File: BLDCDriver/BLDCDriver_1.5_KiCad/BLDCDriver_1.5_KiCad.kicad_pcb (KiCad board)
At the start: 2 copper layers, 42 x 43.2 mm, 72 parts, among them IC1 STSPIN32G4, J2 Debug, J3 FFC_11P_1mm, J4 POWER, J5 CAN, SW1 SW_Push, U4 MCP2562-E-SN, U5 AS5048A-HTSP-500, U6 AP7375-50SA

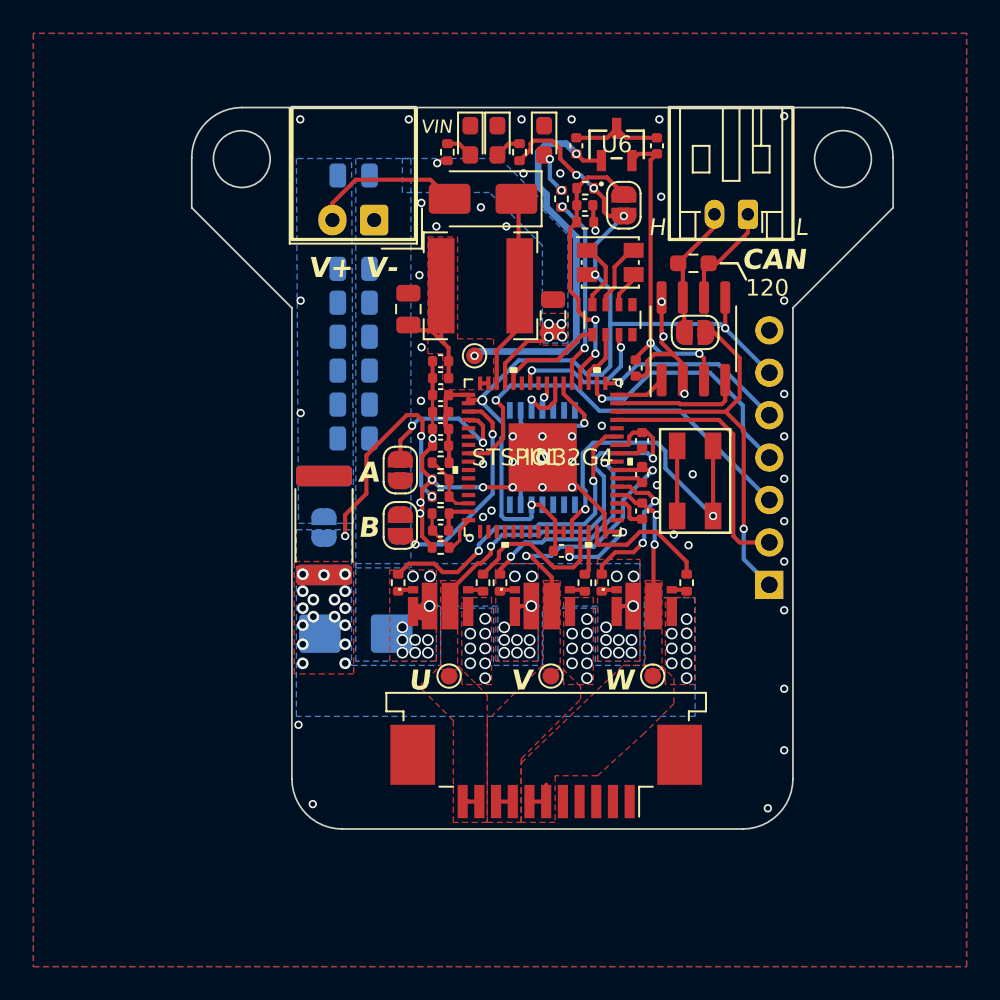
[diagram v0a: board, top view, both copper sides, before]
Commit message: ⚠️電源のシルク逆、SPI_CS繋がってないのを修正、GNDベタ最適化、Production
結構気づかなかったらやばかったやつばっかり
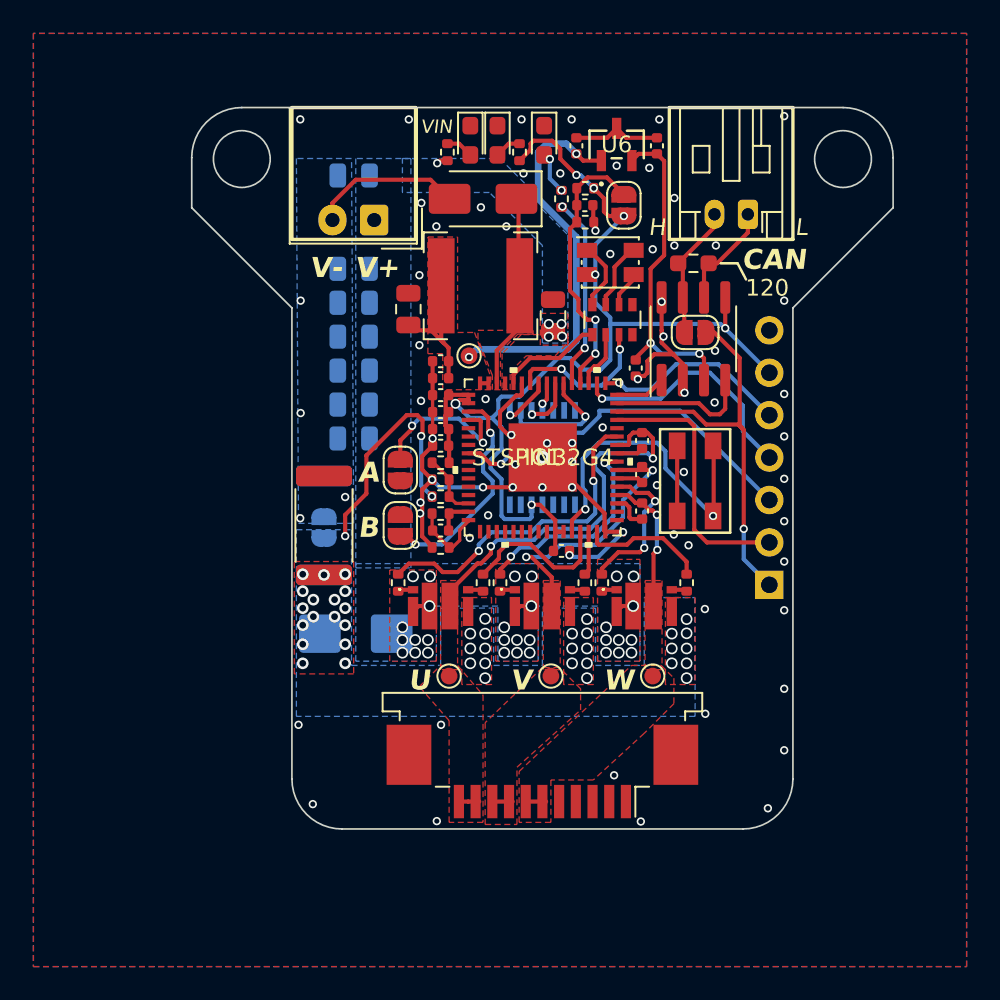
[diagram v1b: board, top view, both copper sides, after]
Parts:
- moved TP1 0.33 mm to (-4.39, -6.10)
- moved J3 0.22 mm to (0.00, 18.8)
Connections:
- IC1 pad 57: SPI1_NSS -> SPI1_CS
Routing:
- net VD: track 9.74 -> 4.35 mm
- net SPI1_CS: track 0.00 -> 2.78 mm, vias 0 -> 1
- net nRST: track 24.5 -> 22.0 mm
- net VDD: track 64.0 -> 65.5 mm
- net OUT3: track 10.4 -> 9.45 mm
- net CAN_RD: track 7.83 -> 8.61 mm
- net GND: track 68.6 -> 69.3 mm, vias 59 -> 75
- net UART_RX: track 25.3 -> 26.0 mm
- net SPI1_MISO: track 3.50 -> 2.96 mm
- added copper zone on F.Cu, net GVCC_SW
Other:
- board text added: "+"
- board text added: "-"

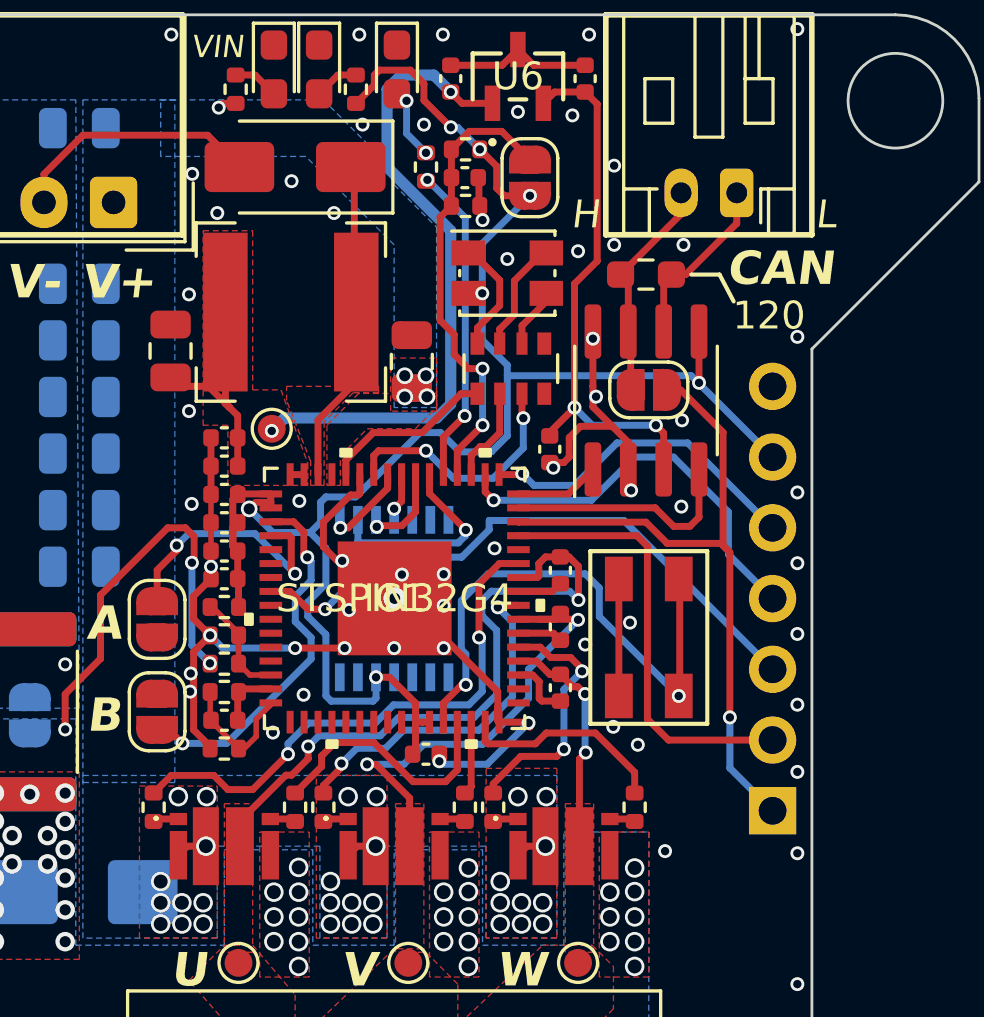
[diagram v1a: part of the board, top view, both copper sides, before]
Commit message: ✏️LEDのRGBの配線を修正・Lチカを確認・DCDCの出力にコンデンサを追加
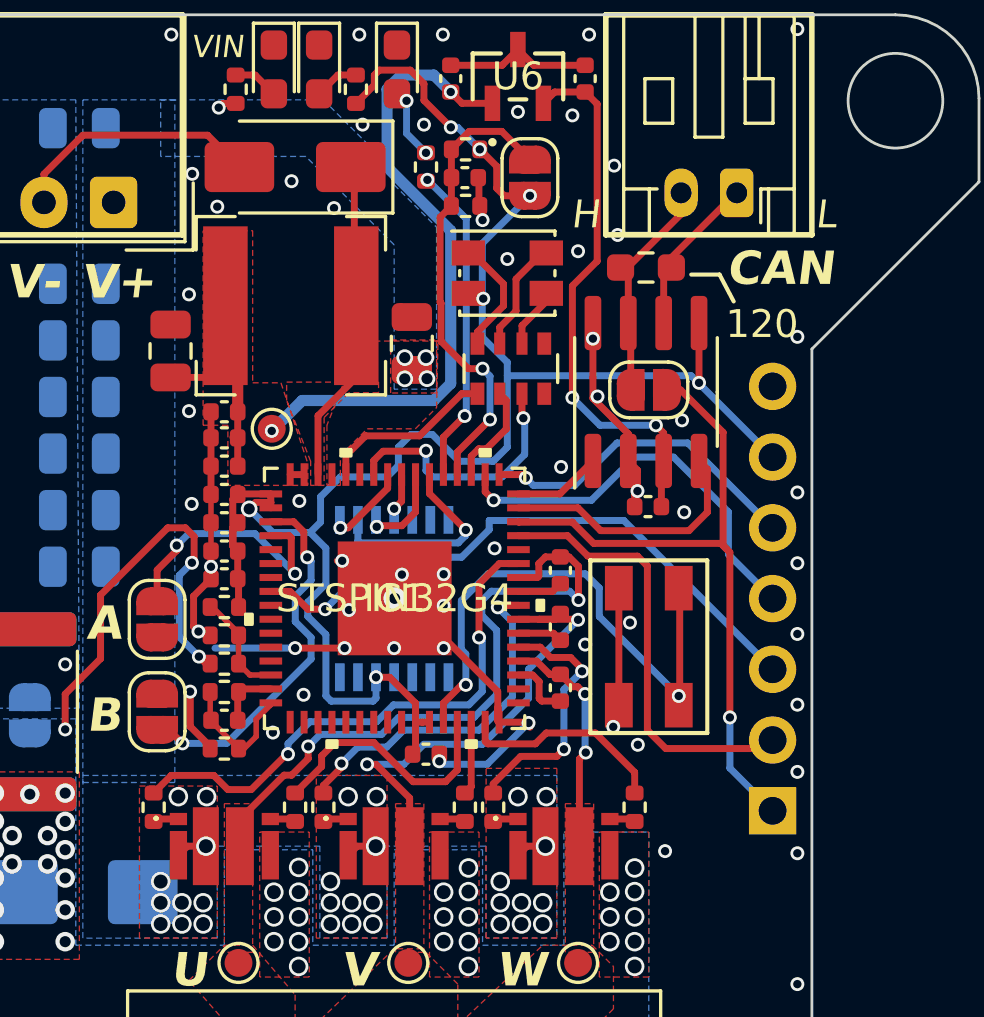
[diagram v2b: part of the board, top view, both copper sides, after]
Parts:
- added C25: 100nF, Capacitor_SMD:C_0402_1005Metric, F.Cu at (-6.10, -6.71)
- moved C23 4.09 mm to (9.12, -3.30), turned to 180 degrees
- moved C10 0.65 mm to (0.64, -9.16)
- moved SW1 0.33 mm to (9.14, 1.73)
- moved U4 0.30 mm to (9.04, -7.42)
- moved R3 0.25 mm to (9.04, -11.9)
- moved L1 0.23 mm to (-3.71, -10.5)
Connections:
- IC1 pad 58: LED_B -> LED_R
- IC1 pad 60: LED_R -> LED_B
- RN1 pad 5: LED_R -> LED_B
- RN1 pad 7: LED_B -> LED_R
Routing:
- net GND: track 69.3 -> 61.2 mm, vias 75 -> 73
- net LED_R: track 6.23 -> 9.43 mm, vias 0 -> 2
- net LED_B: track 8.96 -> 6.33 mm, vias 2 -> 0
- net VCC: track 32.5 -> 34.4 mm
- net VDD: track 65.5 -> 66.4 mm
- net CAN_RD: track 8.61 -> 9.36 mm
- net CANL: track 6.37 -> 5.78 mm

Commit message: ✨フットプリントをMAX3051に変更
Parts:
- removed C21: 10uF, Capacitor_SMD:C_0402_1005Metric
- removed C22: 1uF, Capacitor_SMD:C_0402_1005Metric
- removed C23: 100nF, Capacitor_SMD:C_0402_1005Metric
- removed R3: 120, Resistor_SMD:R_0603_1608Metric_Pad0.98x0.95mm_HandSolder
- removed U4: MCP2562-E-SN, Package_SO:SOIC-8_3.9x4.9mm_P1.27mm
- removed U6: AP7375-50SA, BLDC:AP7375-33SA-7_DIO
- added C26: 100nF, Capacitor_SMD:C_0402_1005Metric, F.Cu at (9.19, -3.20)
- added R20: 120, Resistor_SMD:R_0603_1608Metric_Pad0.98x0.95mm_HandSolder, F.Cu at (9.50, -11.9)
- added U7: MAX3051ESA_, BLDC:SOIC127P600X175-8N, F.Cu at (9.17, -7.42)
- moved JP1 0.15 mm to (5.03, -15.1)
- moved C12 0.10 mm to (2.64, -15.1)
- moved R1 0.08 mm to (2.64, -16.1)
- moved JP5 0.08 mm to (9.14, -7.42)
- moved R2 0.08 mm to (2.64, -14.1)
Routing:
- net VCC: track 34.4 -> 11.2 mm, vias 2 -> 0
- net +5V: track 20.3 -> 0.00 mm, vias 2 -> 0
- net GND: track 61.2 -> 50.5 mm, vias 73 -> 71
- net VDD: track 66.4 -> 70.3 mm, vias 7 -> 8
- net SWCLK: track 14.7 -> 12.9 mm
- net SWDIO: track 11.9 -> 11.0 mm
- net CANH: track 8.27 -> 8.78 mm
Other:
- board text added: "BLDC Driver V1.6"
- board text removed: "BLDC Driver V1.5"
